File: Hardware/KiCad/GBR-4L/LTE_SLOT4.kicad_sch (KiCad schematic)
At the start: 0 parts

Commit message: Add modem and SIM schematics
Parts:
- added C401, C402, C403, C404: 100nF, Capacitor_SMD:C_0603_1608Metric, symbol Device:C
- added C405, C406: 100uF 6.3V low-ESR, Capacitor_SMD:C_1210_3225Metric, symbol Device:C
- added J401: EM7565 M.2 Key B socket, symbol Connector:Bus_M.2_Socket_B
- added J402: MODEM_CONTROL, Connector_PinHeader_2.54mm:PinHeader_1x08_P2.54mm_Vertical, symbol Connector_Generic:Conn_01x08
- added R401: 10k, Resistor_SMD:R_0603_1608Metric, symbol Device:R
- added R402, R403: 100R, Resistor_SMD:R_0603_1608Metric, symbol Device:R
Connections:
- new net +3V3_M4: C401.1, C402.1, C403.1, C404.1, C405.1, C406.1, J401.2 (3.3V), J401.4 (3.3V), J401.70 (3.3V), J401.72 (3.3V), J401.74 (3.3V), J402.1 (Pin_1), R401.1
- new net GND: C401.2, C402.2, C403.2, C404.2, C405.2, C406.2, J401.11 (GND), J401.27 (GND), J401.3 (GND), J401.33 (GND), J401.39 (GND), J401.45 (GND), J401.5 (GND), J401.51 (GND), J401.57 (GND), J401.71 (GND), J401.73 (GND), J402.2 (Pin_2)
- new net M4_FULL_CARD_POWER_OFF#: J401.6 (~{FULL_CARD_POWER_OFF}), J402.4 (Pin_4), R401.2
- new net M4_PWR_EN: J402.3 (Pin_3)
- new net M4_RESET#: J401.67 (~{RESET}), R402.2
- new net M4_RESET_CTRL#: J402.5 (Pin_5), R402.1
- new net M4_SIM_DETECT: J401.66 (SIM_DETECT), J402.8 (Pin_8)
- new net M4_UIM_CLK: J401.32 (UIM-CLK)
- new net M4_UIM_DATA: J401.34 (UIM-DATA)
- new net M4_UIM_PWR: J401.36 (UIM-PWR)
- new net M4_UIM_RESET: J401.30 (UIM-RESET)
- new net M4_WWAN_LED#: J401.10 (GPIO_9/DAS/~{DSS}/~{LED1}), J402.7 (Pin_7)
- new net M4_W_DISABLE#: J401.8 (~{W_DISABLE1}), R403.2
- new net M4_W_DISABLE_CTRL#: J402.6 (Pin_6), R403.1
- new net USB_M4_D+: J401.7 (USB_D+)
- new net USB_M4_D-: J401.9 (USB_D-)
- no-connect marks 0 -> 40
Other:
- note added: "Do not drive module I/O until at least 100 ms after the start of power-up."
- note added: "EM7565 MODEM SLOT 4 — M.2 KEY B 3042"
- note added: "M.2 socket footprint intentionally remains unassigned until the connector height is frozen."
- note added: "Route USB as 90-ohm differential; keep the pair on continuous ground and away from buck switch nodes."
- note added: "USB 2.0 only. PCIe, USB 3.0, secondary SIM, antenna-control and reserved pins are NC."
- title: (none) -> GBR-4L EM7565 slot 4

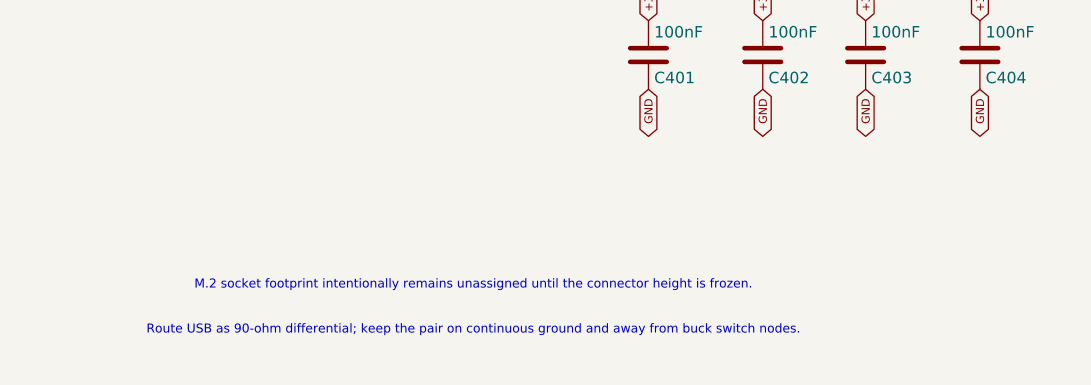
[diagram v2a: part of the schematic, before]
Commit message: Add connector footprints and initial PCB packing
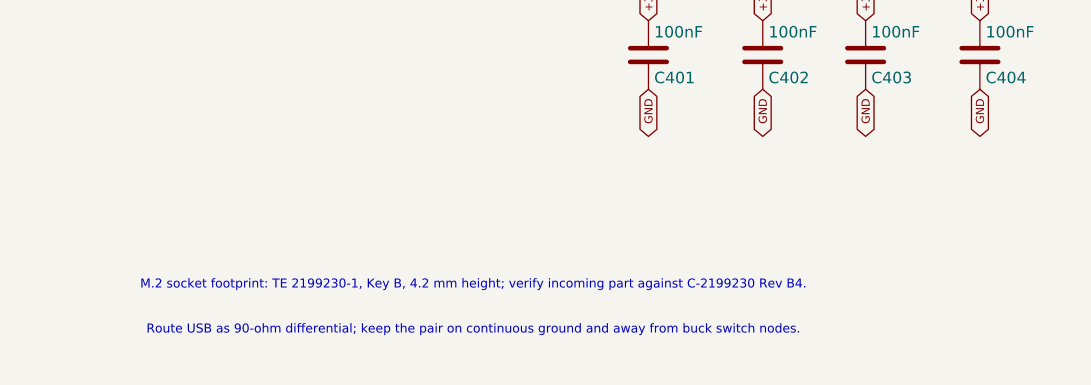
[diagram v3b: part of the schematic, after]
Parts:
- J401: footprint (none) -> GBR-4L:TE_2199230-1_M2_Key-B
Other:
- note added: "M.2 socket footprint: TE 2199230-1, Key B, 4.2 mm height; verify incoming part against C-2199230 Rev B4."
- note removed: "M.2 socket footprint intentionally remains unassigned until the connector height is frozen."
